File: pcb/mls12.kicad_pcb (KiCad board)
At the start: 4 copper layers, 130 x 40 mm, 139 parts, among them J1 MTJ-88ARX1-FSM-LG, J2 TC2070-FP, J3 SM04B-SRSS-TB, J4 JST B3B-ZR, J5 DC barrel plug, J6 JST B3B-ZR, J7 DC barrel plug, Q1 DMG3406L, Q2 DMG3406L, Q3 DMG3406L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

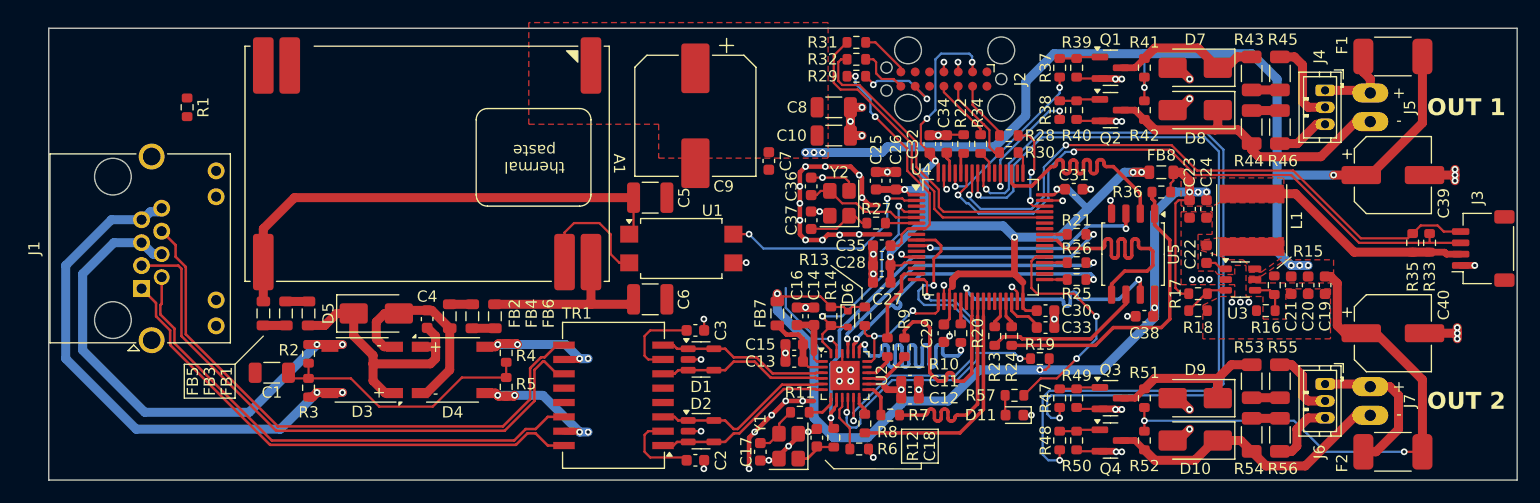
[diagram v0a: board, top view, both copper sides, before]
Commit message: Ground return vias
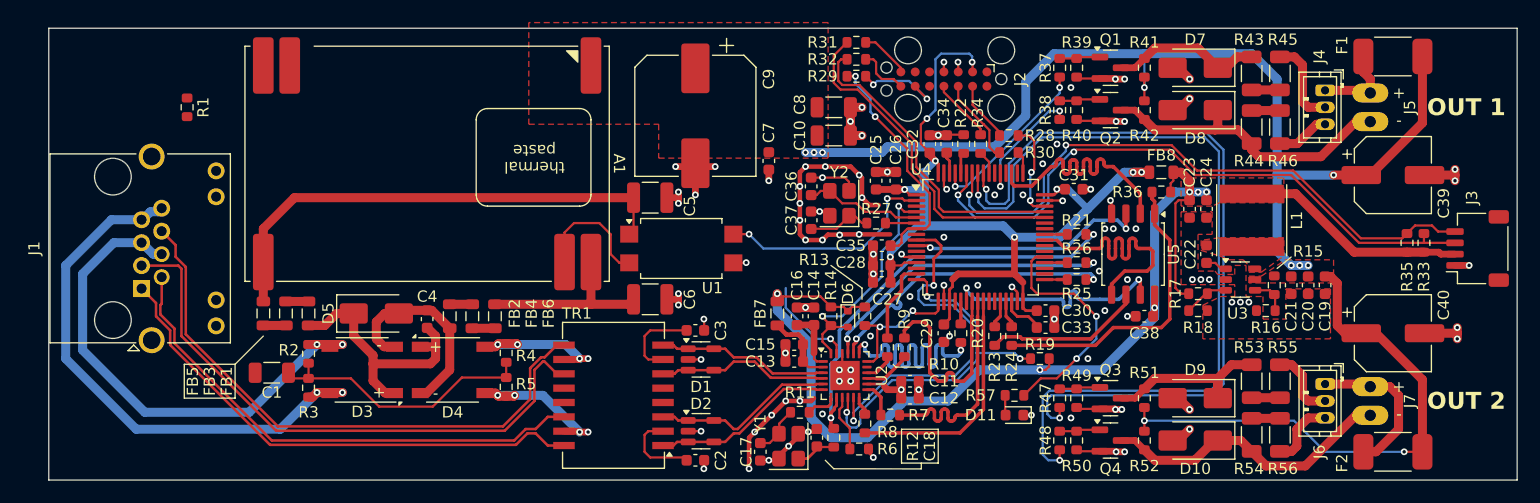
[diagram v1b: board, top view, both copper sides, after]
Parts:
- moved J3 0.50 mm to (236.5, 99.5)
- moved R33 0.50 mm to (231.8, 99.0)
- moved R35 0.50 mm to (230.2, 99.0)
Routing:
- net GND: track 117.0 -> 130.4 mm, vias 79 -> 103
- net /LED output 2/PWM_WW: track 67.2 -> 69.1 mm
- net /LED output 2/PWM_CW: track 71.7 -> 73.4 mm

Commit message: Add mounting holes, round corners
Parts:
- added H1: M2.5, MountingHole:MountingHole_2.7mm_M2.5_ISO7380, F.Cu at (114.0, 84.0)
- added H2: M2.5, MountingHole:MountingHole_2.7mm_M2.5_ISO7380, F.Cu at (114.0, 116.0)
- added H3: M2.5, MountingHole:MountingHole_2.7mm_M2.5_ISO7380, F.Cu at (230.0, 100.0)
- moved R33 5.52 mm to (226.2, 98.5)
- moved R35 5.52 mm to (224.8, 98.5)
- moved J3 0.50 mm to (236.5, 100.0)
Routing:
- net +3.3V: track 116.3 -> 119.2 mm
- net /MCU/SDA: track 55.6 -> 57.3 mm
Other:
- outline, holes or cut-outs redrawn

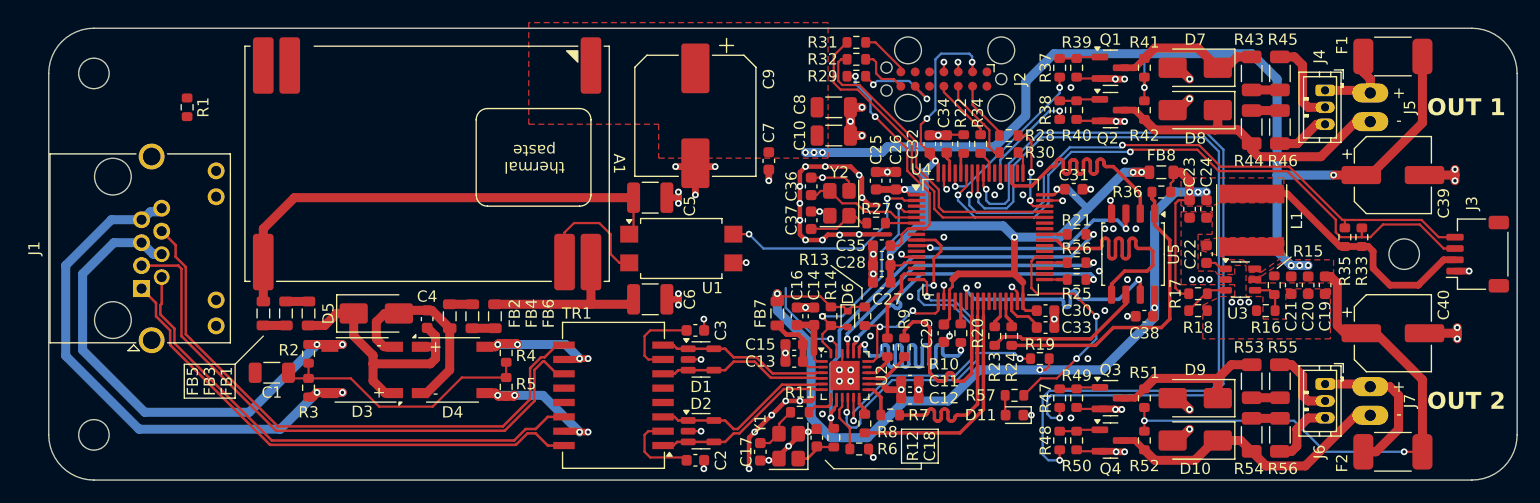
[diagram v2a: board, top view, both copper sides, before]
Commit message: Add power planes, fiducials
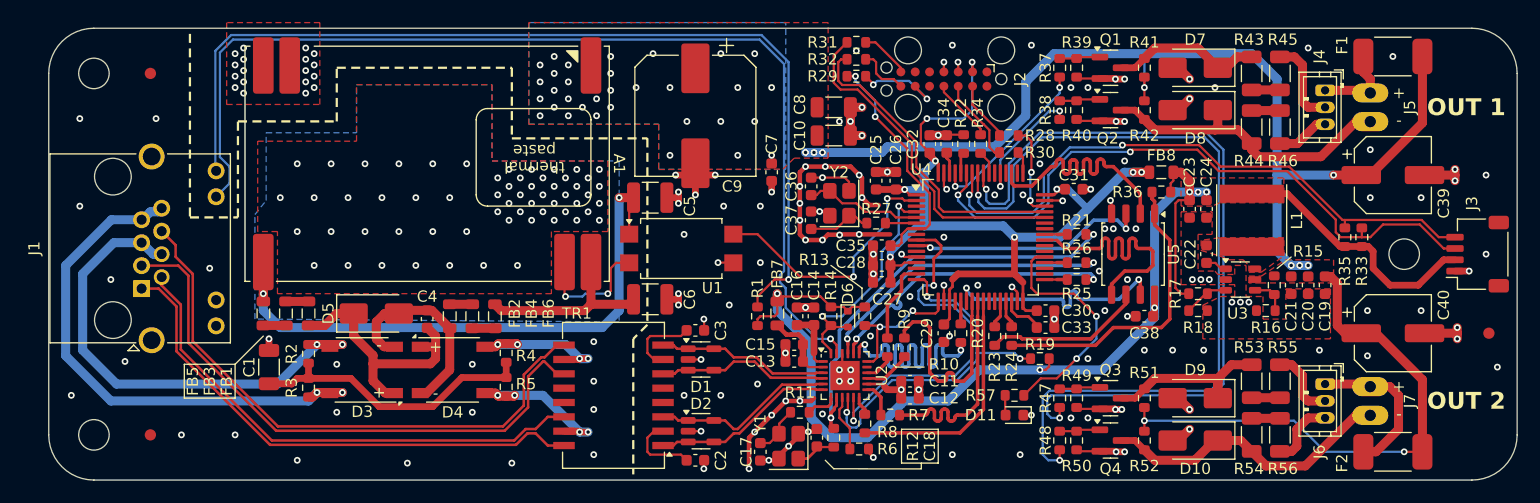
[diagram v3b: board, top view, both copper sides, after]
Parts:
- added FID1: 1MM, Fiducial:Fiducial_1mm_Mask2mm, F.Cu at (119.0, 84.0)
- added FID2: 1MM, Fiducial:Fiducial_1mm_Mask2mm, F.Cu at (119.0, 116.0)
- added FID3: 1MM, Fiducial:Fiducial_1mm_Mask2mm, F.Cu at (237.5, 107.0)
- moved R1 53.8 mm to (172.8, 105.5), turned to 90 degrees
- moved C7 1.03 mm to (174.0, 92.8)
- moved C1 0.56 mm to (129.5, 110.0), turned to 90 degrees
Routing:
- net Net-(J1-Pad12): track 0.00 -> 86.5 mm, vias 0 -> 1
- net /ETH-CONN/LED0: track 8.39 -> 93.5 mm
- net Net-(A1-V_{IN+}): track 43.7 -> 52.4 mm, vias 0 -> 2
- net +3.3V: track 119.2 -> 122.8 mm
- net /ETH-PoE+/TYP2_DET: track 19.9 -> 23.0 mm
- net /ETH-CONN/V_{INB}: track 50.4 -> 48.3 mm
- net /ETH-CONN/V_{INA}: track 46.3 -> 44.2 mm
- net Net-(C1-Pad1): track 24.3 -> 26.0 mm
- net /MCU/V_{t,ref}: track 84.6 -> 83.5 mm
- net GNDPWR: track 0.00 -> 1.03 mm, vias 0 -> 81
- net /ETH-CONN/MDI_TX+: track 45.4 -> 46.3 mm
- net GND: track 130.4 -> 131.3 mm, vias 103 -> 153
- net Net-(TR1-CRD): track 7.45 -> 6.66 mm
- net /ETH-CONN/V_{IND}: track 13.0 -> 13.7 mm
- net /ETH-CONN/V_{INC}: track 13.5 -> 14.3 mm
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- added copper zone on B.Cu, net +24V
- added copper zone on In2.Cu, net GND
- added copper zone on B.Cu, net GNDPWR
- added copper zone on F.Cu, net GNDPWR
- added copper zone on In1.Cu, net GNDPWR
- added copper zone on In2.Cu, net GNDPWR

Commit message: Add test points
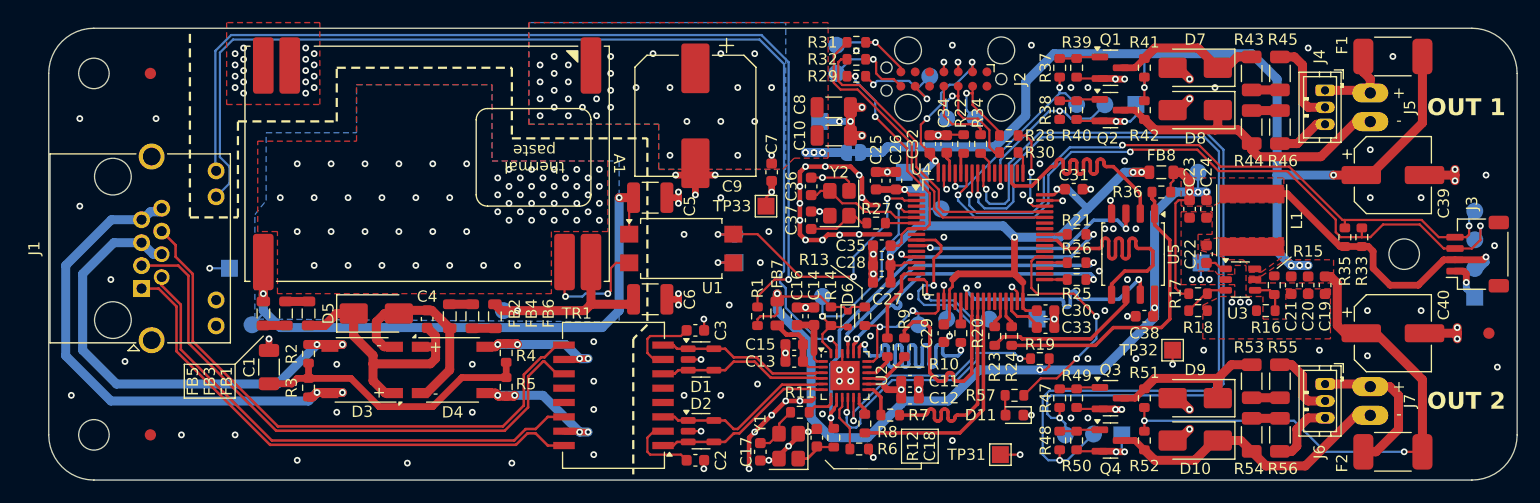
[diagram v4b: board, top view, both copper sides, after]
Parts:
- added JP1: SolderJumper_2_Bridged, Jumper:SolderJumper-2_P1.3mm_Bridged_RoundedPad1.0x1.5mm, B.Cu at (181.2, 91.0)
- added TP1: TestPoint, TestPoint:TestPoint_Pad_1.5x1.5mm, B.Cu at (178.2, 88.2)
- added TP10: TestPoint, TestPoint:TestPoint_Pad_D1.5mm, B.Cu at (193.2, 105.8)
- added TP11: TestPoint, TestPoint:TestPoint_Pad_1.5x1.5mm, B.Cu at (197.5, 105.8)
- added TP12: TestPoint, TestPoint:TestPoint_Pad_D1.5mm, B.Cu at (187.0, 106.2)
- added TP13: TestPoint, TestPoint:TestPoint_Pad_D1.5mm, B.Cu at (178.5, 103.8)
- added TP14: TestPoint, TestPoint:TestPoint_Pad_1.5x1.5mm, B.Cu at (236.2, 103.8)
- added TP15: TestPoint, TestPoint:TestPoint_Pad_D1.5mm, B.Cu at (236.2, 101.3)
- added TP16: TestPoint, TestPoint:TestPoint_Pad_D1.5mm, B.Cu at (236.2, 98.7)
- added TP17: TestPoint, TestPoint:TestPoint_Pad_D1.5mm, B.Cu at (236.2, 96.2)
- added TP18: TestPoint, TestPoint:TestPoint_Pad_D1.5mm, B.Cu at (188.0, 84.2)
- added TP19: TestPoint, TestPoint:TestPoint_Pad_D1.5mm, B.Cu at (192.0, 88.0)
- added TP2: TestPoint, TestPoint:TestPoint_Pad_D1.5mm, B.Cu at (211.8, 92.8)
- added TP20: TestPoint, TestPoint:TestPoint_Pad_D1.5mm, B.Cu at (189.5, 88.0)
- added TP21: TestPoint, TestPoint:TestPoint_Pad_D1.5mm, B.Cu at (179.8, 81.5)
- added TP22: TestPoint, TestPoint:TestPoint_Pad_D1.5mm, B.Cu at (179.8, 84.0)
- added TP23: TestPoint, TestPoint:TestPoint_Pad_D1.5mm, B.Cu at (189.0, 96.0)
- added TP24: TestPoint, TestPoint:TestPoint_Pad_1.5x1.5mm, B.Cu at (185.8, 92.8)
- added TP25: TestPoint, TestPoint:TestPoint_Pad_D1.5mm, B.Cu at (201.0, 86.8)
- added TP26: TestPoint, TestPoint:TestPoint_Pad_1.5x1.5mm, B.Cu at (206.2, 86.8)
- added TP27: TestPoint, TestPoint:TestPoint_Pad_D1.5mm, B.Cu at (200.0, 116.0)
- added TP28: TestPoint, TestPoint:TestPoint_Pad_1.5x1.5mm, B.Cu at (205.0, 116.0)
- added TP29: TestPoint, TestPoint:TestPoint_Pad_D1.5mm, B.Cu at (203.5, 86.8)
- added TP3: TestPoint, TestPoint:TestPoint_Pad_1.5x1.5mm, B.Cu at (212.0, 100.8)
- added TP30: TestPoint, TestPoint:TestPoint_Pad_D1.5mm, B.Cu at (202.5, 115.9)
- added TP31: TestPoint, TestPoint:TestPoint_Pad_1.5x1.5mm, F.Cu at (194.2, 117.8)
- added TP32: TestPoint, TestPoint:TestPoint_Pad_1.5x1.5mm, F.Cu at (209.5, 108.5)
- added TP33: TestPoint, TestPoint:TestPoint_Pad_1.5x1.5mm, F.Cu at (173.5, 95.8)
- added TP4: TestPoint, TestPoint:TestPoint_Pad_D1.5mm, B.Cu at (128.0, 106.2)
- added TP5: TestPoint, TestPoint:TestPoint_Pad_D1.5mm, B.Cu at (150.2, 105.0)
- added TP6: TestPoint, TestPoint:TestPoint_Pad_1.5x1.5mm, B.Cu at (126.0, 101.2)
- added TP7: TestPoint, TestPoint:TestPoint_Pad_D1.5mm, B.Cu at (170.8, 98.2)
- added TP8: TestPoint, TestPoint:TestPoint_Pad_1.5x1.5mm, B.Cu at (170.8, 100.8)
- added TP9: TestPoint, TestPoint:TestPoint_Pad_D1.5mm, B.Cu at (189.5, 105.8)
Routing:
- net GND: track 131.3 -> 150.5 mm
- net +3.3V: track 122.8 -> 129.1 mm, vias 7 -> 8
- net /MCU/SDA: track 57.3 -> 62.6 mm, vias 2 -> 3
- net /LED output 1/PWM_CW: track 11.3 -> 16.1 mm
- net /LED output 2/PWM_CW: track 73.4 -> 77.4 mm
- net Net-(J2-RX): track 4.69 -> 8.46 mm, vias 0 -> 1
- net Net-(J2-TX): track 4.41 -> 8.09 mm, vias 0 -> 1
- net /MCU/SCL: track 54.3 -> 57.9 mm, vias 2 -> 3
- net Net-(J2-SWCLK): track 7.64 -> 11.1 mm, vias 0 -> 1
- net Net-(J2-SWDIO): track 5.35 -> 8.45 mm, vias 0 -> 1
- net /ETH-PoE+/TYP2_DET: track 23.0 -> 25.9 mm, vias 2 -> 3
- net /LED output 1/PWM_WW: track 15.3 -> 17.2 mm
- net GNDPWR: track 1.03 -> 2.78 mm
- net /ETH-PHY/~{RST}: track 21.1 -> 22.9 mm
- net /LED output 2/PWM_WW: track 69.1 -> 70.8 mm
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
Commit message: Cleanup silkscreen, add logo
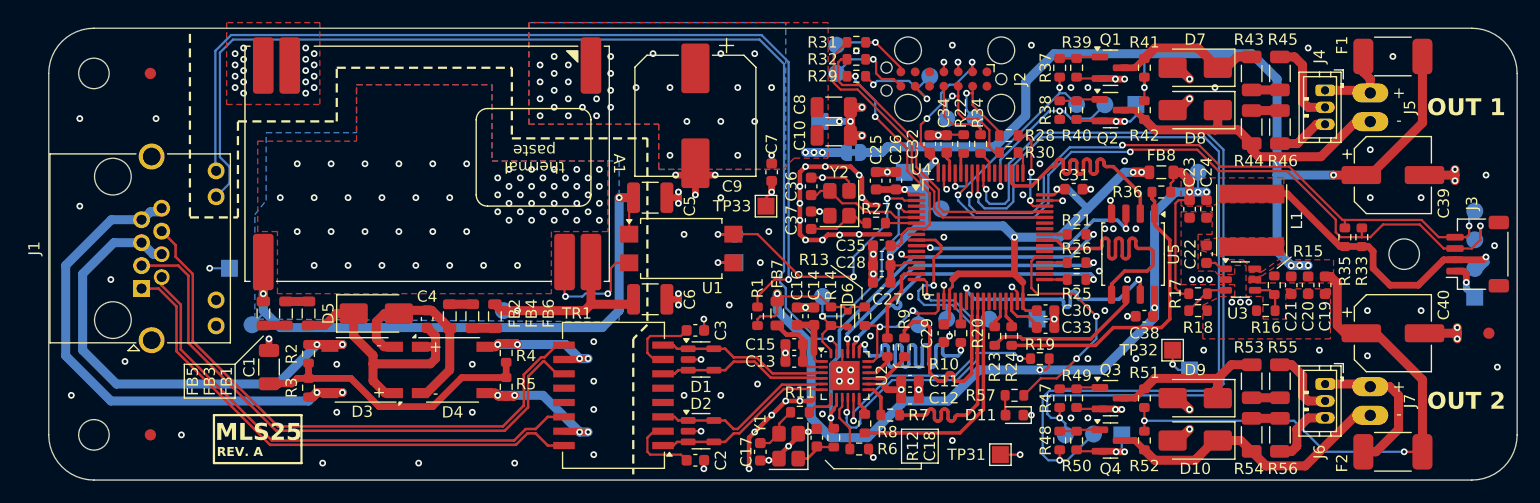
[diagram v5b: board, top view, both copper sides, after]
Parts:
- moved TP3 9.53 mm to (211.0, 110.2)
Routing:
- net GNDPWR: vias 81 -> 80
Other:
- board text added: "MLS25"
- board text added: "REV. A"
